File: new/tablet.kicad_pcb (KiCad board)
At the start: 2 copper layers, 15 parts, among them J1 Conn_02x20_Odd_Even, J2 USB_B_Micro, J3 Conn_02x04_Odd_Even, J4 Conn_02x04_Odd_Even, U1 STM32F429Z_E-G_Tx

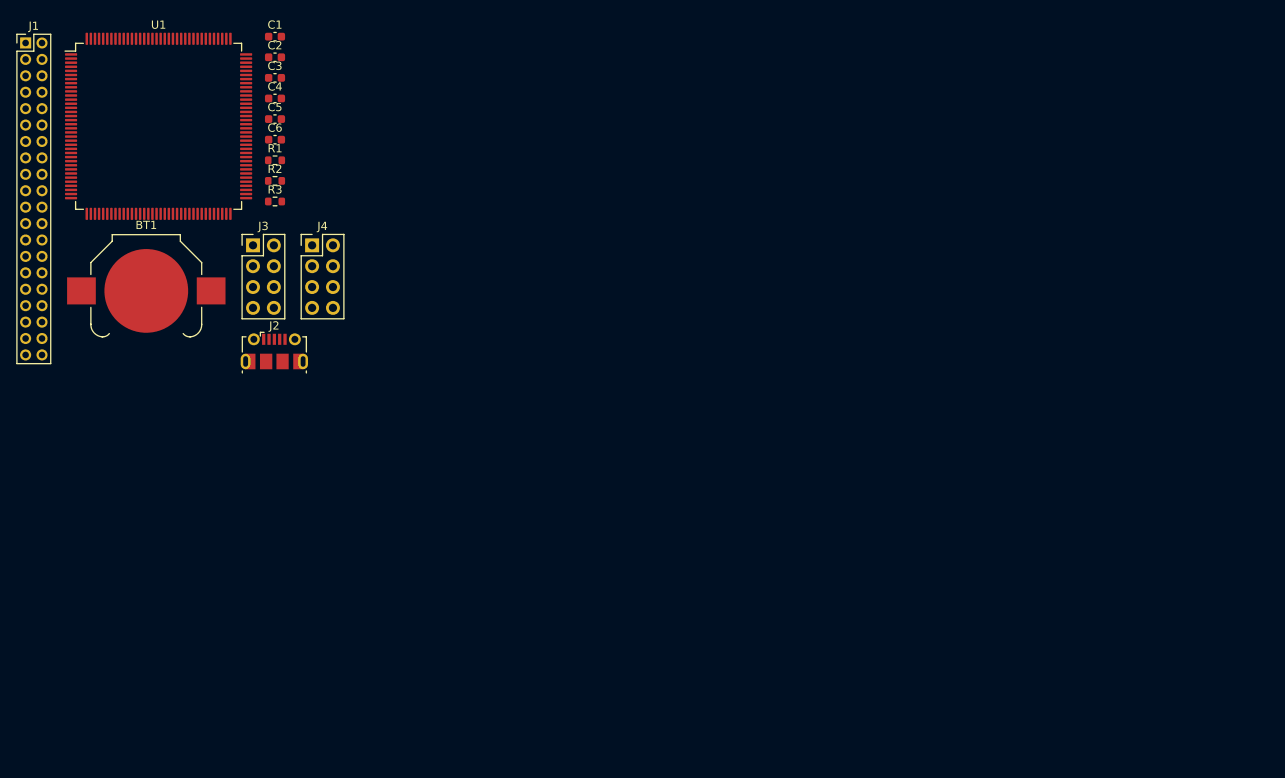
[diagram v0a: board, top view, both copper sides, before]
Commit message: place header on pcb
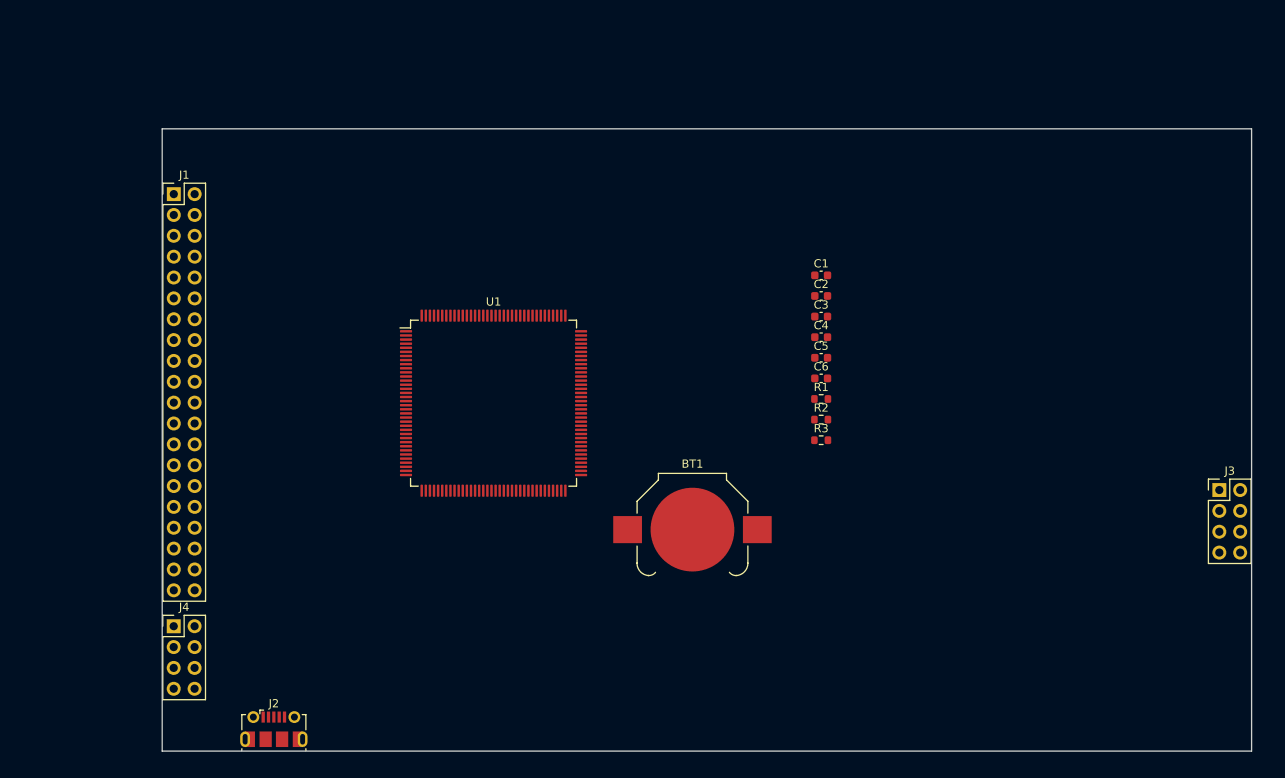
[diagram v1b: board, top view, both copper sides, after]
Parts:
- J1: footprint Connector_PinHeader_2.00mm:PinHeader_2x20_P2.00mm_Vertical -> Connector_PinHeader_2.54mm:PinHeader_2x20_P2.54mm_Vertical
- moved J3 121.4 mm to (261.5, 119.8)
- moved BT1 72.6 mm to (197.3, 124.6)
- moved C1 72.6 mm to (213.0, 93.7)
- moved C2 72.6 mm to (213.0, 96.2)
- moved C3 72.6 mm to (213.0, 98.7)
- moved C4 72.6 mm to (213.0, 101.2)
- moved C5 72.6 mm to (213.0, 103.7)
- moved C6 72.6 mm to (213.0, 106.2)
- moved R1 72.6 mm to (213.0, 108.7)
- moved R2 72.6 mm to (213.0, 111.2)
- moved R3 72.6 mm to (213.0, 113.7)
- moved U1 52.9 mm to (173.1, 109.2)
- moved J4 49.4 mm to (134.1, 136.4)
- moved J2 46.0 mm to (146.3, 148.9)
- moved J1 25.8 mm to (134.1, 83.8)
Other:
- board outline added: 132.7 x 75.8 mm

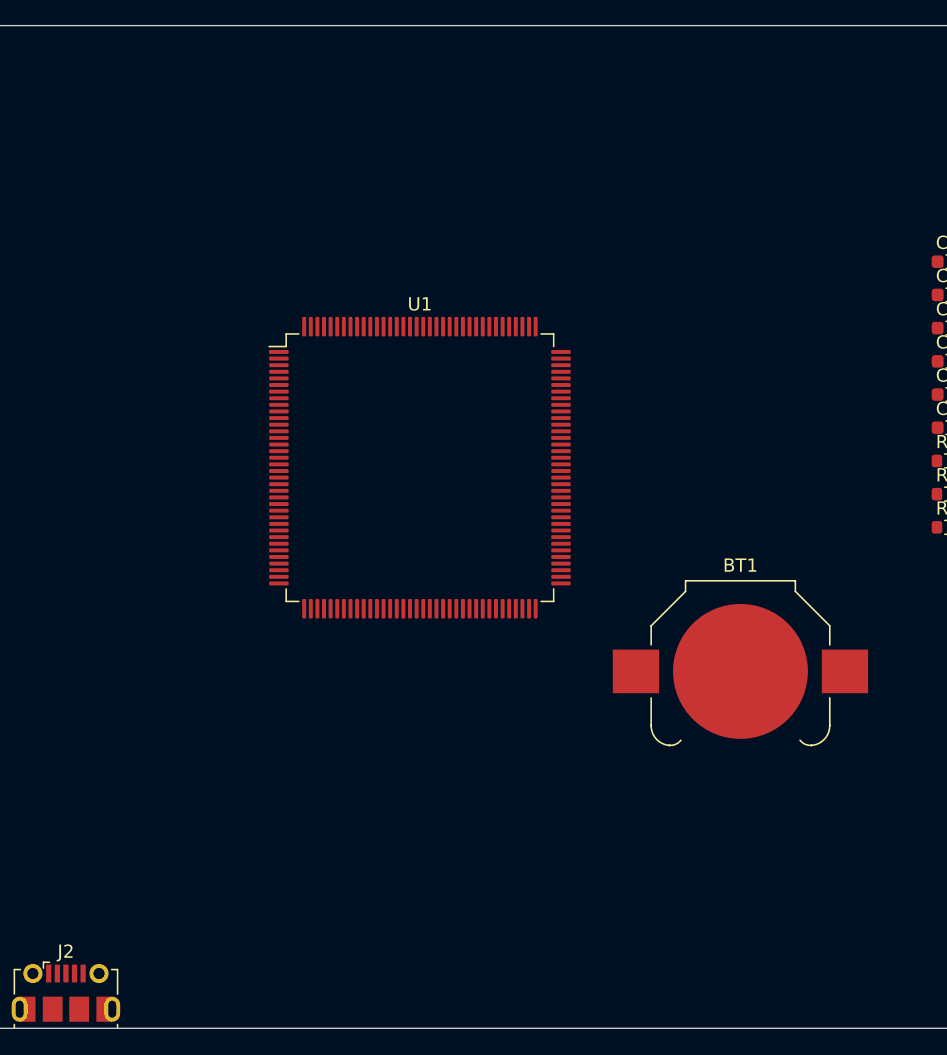
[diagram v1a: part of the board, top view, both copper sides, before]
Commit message: add TPS63001
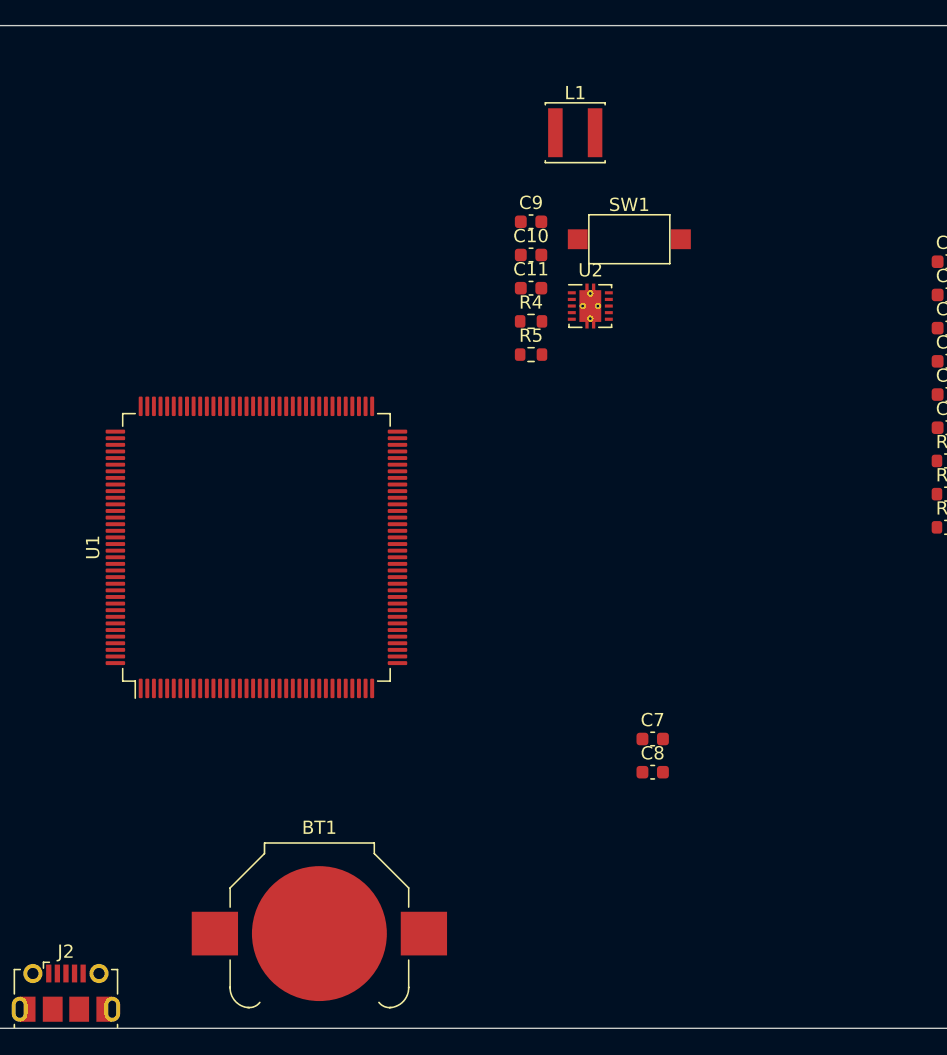
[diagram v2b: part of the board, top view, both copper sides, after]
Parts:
- added C10: 0.1uF, Capacitor_SMD:C_0603_1608Metric, F.Cu at (181.5, 93.1)
- added C11: 0.1uF, Capacitor_SMD:C_0603_1608Metric, F.Cu at (181.5, 95.7)
- added C7: 2.2uF, Capacitor_SMD:C_0603_1608Metric, F.Cu at (190.7, 129.7)
- added C8: 2.2uF, Capacitor_SMD:C_0603_1608Metric, F.Cu at (190.7, 132.2)
- added C9: 0.1uF, Capacitor_SMD:C_0603_1608Metric, F.Cu at (181.5, 90.6)
- added L1: LPS4012-103MRB, Inductor_SMD:L_Sunlord_SWPA4012S, F.Cu at (184.8, 83.9)
- added R4: 10k, Resistor_SMD:R_0603_1608Metric, F.Cu at (181.5, 98.2)
- added R5: 100, Resistor_SMD:R_0603_1608Metric, F.Cu at (181.5, 100.7)
- added SW1: SW_SPST, Button_Switch_SMD:SW_SPST_CK_RS282G05A3, F.Cu at (188.9, 92.0)
- added U2: TPS63001, Package_SON:Texas_DRC0010J_ThermalVias, F.Cu at (185.9, 97.0)
- J1: value Conn_02x20_Odd_Even -> FSMC/TOUCH-SPI
- J3: value Conn_02x04_Odd_Even -> SD/CARD
- J4: value Conn_02x04_Odd_Even -> FLASH/FONT
- moved BT1 37.5 mm to (165.5, 144.4)
- moved U1 13.7 mm to (160.7, 115.2), turned to 90 degrees
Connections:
- J1 pad 1: unconnected-(J1-Pin_1-Pad1) -> GND
- J1 pad 17: unconnected-(J1-Pin_17-Pad17) -> PD10-D15
- J1 pad 18: unconnected-(J1-Pin_18-Pad18) -> PD9-D14
- J1 pad 19: unconnected-(J1-Pin_19-Pad19) -> PD8-D13
- J1 pad 2: unconnected-(J1-Pin_2-Pad2) -> PA10-BL
- J1 pad 20: unconnected-(J1-Pin_20-Pad20) -> PE15-D12
- J1 pad 21: unconnected-(J1-Pin_21-Pad21) -> PE14-D11
- J1 pad 22: unconnected-(J1-Pin_22-Pad22) -> PE13-D10
- J1 pad 23: unconnected-(J1-Pin_23-Pad23) -> PE12-D9
- J1 pad 24: unconnected-(J1-Pin_24-Pad24) -> PE11-D8
- J1 pad 25: unconnected-(J1-Pin_25-Pad25) -> PE10-D7
- J1 pad 26: unconnected-(J1-Pin_26-Pad26) -> PE9-D6
- J1 pad 27: unconnected-(J1-Pin_27-Pad27) -> PE8-D5
- J1 pad 28: unconnected-(J1-Pin_28-Pad28) -> PE7-D4
- J1 pad 29: unconnected-(J1-Pin_29-Pad29) -> PD1-D3
- J1 pad 3: unconnected-(J1-Pin_3-Pad3) -> PD6-TP/IRQ
- J1 pad 30: unconnected-(J1-Pin_30-Pad30) -> PD0-D2
- J1 pad 31: unconnected-(J1-Pin_31-Pad31) -> PD15-D1
- J1 pad 32: unconnected-(J1-Pin_32-Pad32) -> PD14-D0
- J1 pad 33: unconnected-(J1-Pin_33-Pad33) -> TE
- J1 pad 34: unconnected-(J1-Pin_34-Pad34) -> TFT-RESET
- J1 pad 35: unconnected-(J1-Pin_35-Pad35) -> PD5-/WR
- J1 pad 36: unconnected-(J1-Pin_36-Pad36) -> PD4-/RD
- J1 pad 37: unconnected-(J1-Pin_37-Pad37) -> PD11-RS
- J1 pad 38: unconnected-(J1-Pin_38-Pad38) -> PD7-/CS
- J1 pad 39: unconnected-(J1-Pin_39-Pad39) -> +3V3
- J1 pad 40: unconnected-(J1-Pin_40-Pad40) -> GND
- J1 pad 5: unconnected-(J1-Pin_5-Pad5) -> PB14-SO
- J1 pad 6: unconnected-(J1-Pin_6-Pad6) -> PB15-SI
- J1 pad 7: unconnected-(J1-Pin_7-Pad7) -> PB13-TP/SCK
- J1 pad 8: unconnected-(J1-Pin_8-Pad8) -> PB12-TP/CS
- J3 pad 1: unconnected-(J3-Pin_1-Pad1) -> PC11-DAT3
- J3 pad 2: unconnected-(J3-Pin_2-Pad2) -> PC10-DAT2
- J3 pad 3: unconnected-(J3-Pin_3-Pad3) -> PC12-CLK
- J3 pad 4: unconnected-(J3-Pin_4-Pad4) -> PD2-CMD
- J3 pad 5: unconnected-(J3-Pin_5-Pad5) -> PC8-DAT0
- J3 pad 6: unconnected-(J3-Pin_6-Pad6) -> GND
- J3 pad 7: unconnected-(J3-Pin_7-Pad7) -> PC0-SDDETECT
- J3 pad 8: unconnected-(J3-Pin_8-Pad8) -> PC9-DAT1
- U1 pad 102: unconnected-(U1-PA10-Pad102) -> PA10-BL
- U1 pad 106: unconnected-(U1-VCAP_2-Pad106) -> Net-(U1-VCAP_2)
- U1 pad 111: unconnected-(U1-PC10-Pad111) -> PC10-DAT2
- U1 pad 112: unconnected-(U1-PC11-Pad112) -> PC11-DAT3
- U1 pad 113: unconnected-(U1-PC12-Pad113) -> PC12-CLK
- U1 pad 114: unconnected-(U1-PD0-Pad114) -> PD0-D2
- U1 pad 115: unconnected-(U1-PD1-Pad115) -> PD1-D3
- U1 pad 116: unconnected-(U1-PD2-Pad116) -> PD2-CMD
- U1 pad 118: unconnected-(U1-PD4-Pad118) -> PD4-/RD
- U1 pad 119: unconnected-(U1-PD5-Pad119) -> PD5-/WR
- U1 pad 122: unconnected-(U1-PD6-Pad122) -> PD6-TP/IRQ
- U1 pad 123: unconnected-(U1-PD7-Pad123) -> PD7-/CS
- U1 pad 138: unconnected-(U1-BOOT0-Pad138) -> BOOT0
- U1 pad 143: unconnected-(U1-PDR_ON-Pad143) -> +3V3
- U1 pad 25: unconnected-(U1-NRST-Pad25) -> Net-(U1-NRST)
- U1 pad 26: unconnected-(U1-PC0-Pad26) -> PC0-SDDETECT
- U1 pad 48: unconnected-(U1-PB2-Pad48) -> BOOT1
- U1 pad 58: unconnected-(U1-PE7-Pad58) -> PE7-D4
- U1 pad 59: unconnected-(U1-PE8-Pad59) -> PE8-D5
- U1 pad 60: unconnected-(U1-PE9-Pad60) -> PE9-D6
- U1 pad 63: unconnected-(U1-PE10-Pad63) -> PE10-D7
- U1 pad 64: unconnected-(U1-PE11-Pad64) -> PE11-D8
- U1 pad 65: unconnected-(U1-PE12-Pad65) -> PE12-D9
- U1 pad 66: unconnected-(U1-PE13-Pad66) -> PE13-D10
- U1 pad 67: unconnected-(U1-PE14-Pad67) -> PE14-D11
- U1 pad 68: unconnected-(U1-PE15-Pad68) -> PE15-D12
- U1 pad 71: unconnected-(U1-VCAP_1-Pad71) -> Net-(U1-VCAP_1)
- U1 pad 73: unconnected-(U1-PB12-Pad73) -> PB12-TP/CS
- U1 pad 74: unconnected-(U1-PB13-Pad74) -> PB13-TP/SCK
- U1 pad 75: unconnected-(U1-PB14-Pad75) -> PB14-SO
- U1 pad 76: unconnected-(U1-PB15-Pad76) -> PB15-SI
- U1 pad 77: unconnected-(U1-PD8-Pad77) -> PD8-D13
- U1 pad 78: unconnected-(U1-PD9-Pad78) -> PD9-D14
- U1 pad 79: unconnected-(U1-PD10-Pad79) -> PD10-D15
- U1 pad 80: unconnected-(U1-PD11-Pad80) -> PD11-RS
- U1 pad 85: unconnected-(U1-PD14-Pad85) -> PD14-D0
- U1 pad 98: unconnected-(U1-PC8-Pad98) -> PC8-DAT0
- U1 pad 99: unconnected-(U1-PC9-Pad99) -> PC9-DAT1

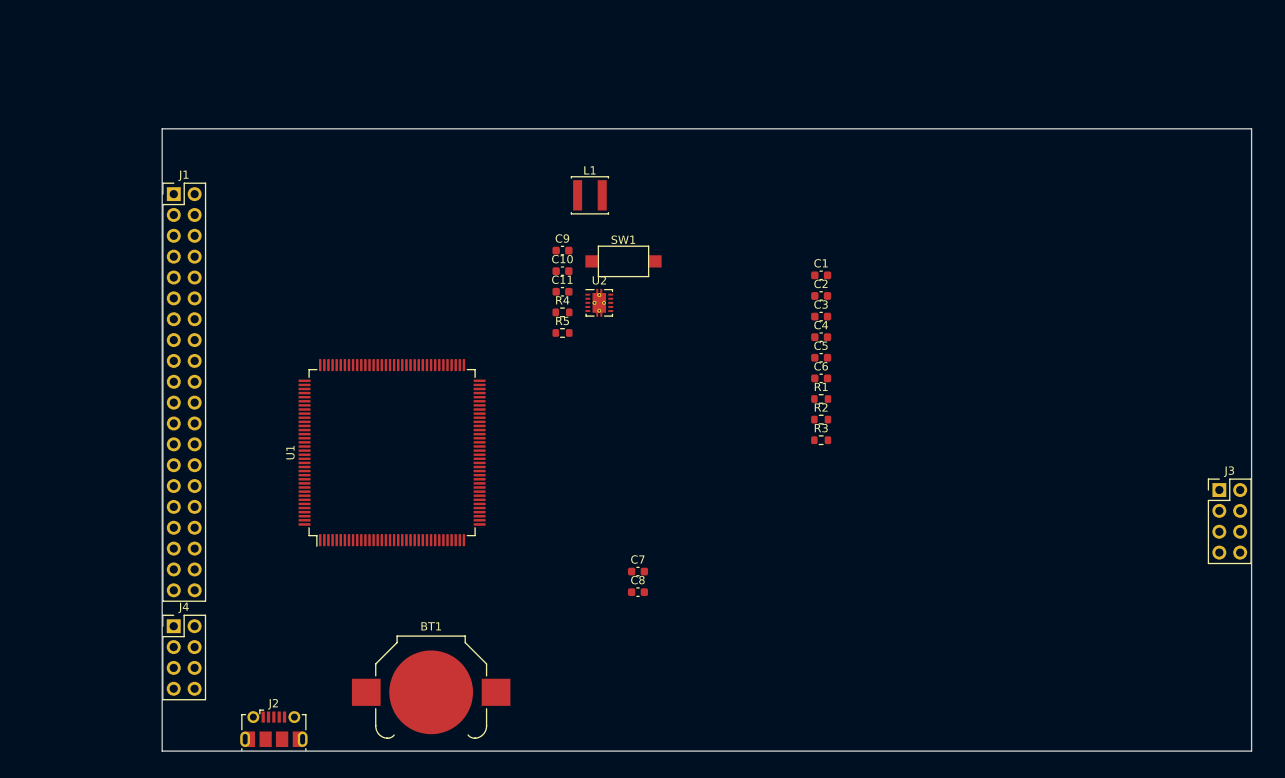
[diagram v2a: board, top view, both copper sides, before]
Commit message: add wiring + battery charging
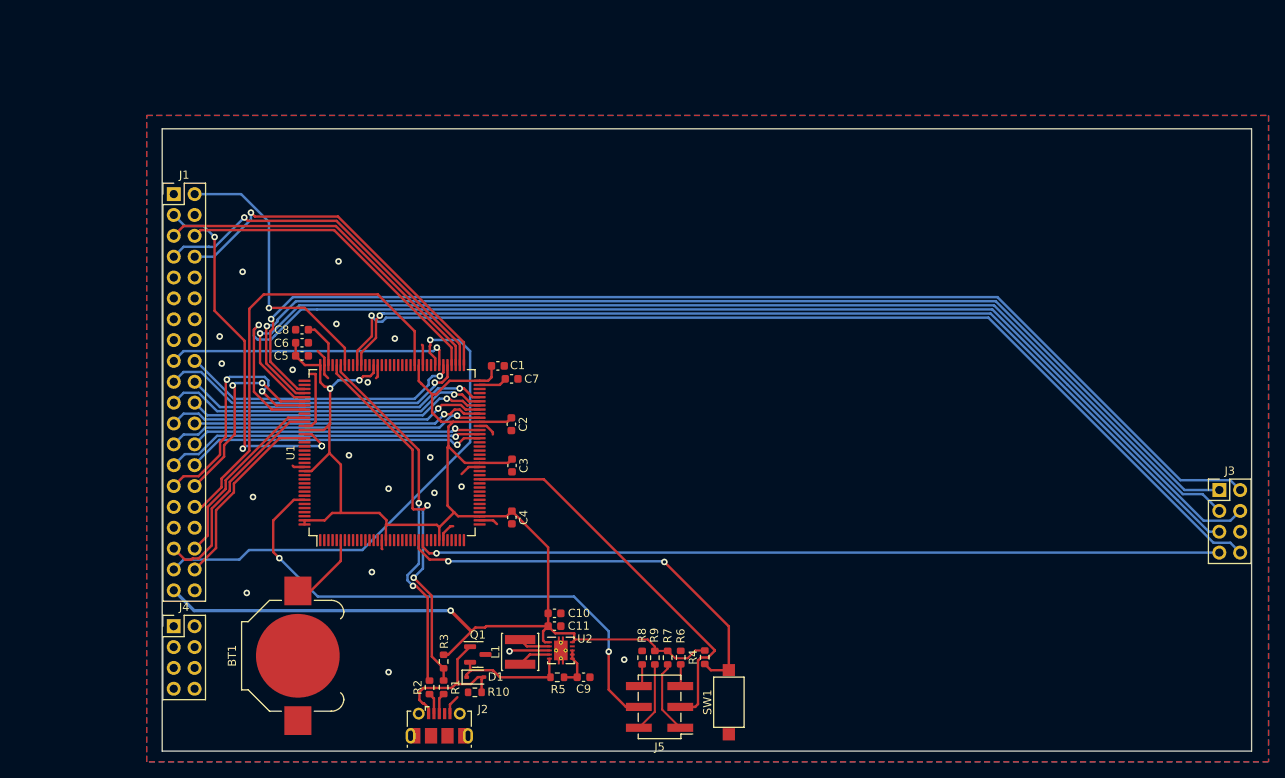
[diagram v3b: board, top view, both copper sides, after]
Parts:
- added D1: BAT48JFILM, Diode_SMD:D_SOD-323, F.Cu at (170.8, 142.6)
- added J5: Conn_02x03_Odd_Even, Connector_PinHeader_2.54mm:PinHeader_2x03_P2.54mm_Vertical_SMD, F.Cu at (193.3, 146.2)
- added Q1: DMG2301L, Package_TO_SOT_SMD:SOT-23, F.Cu at (171.1, 139.8)
- added R10: 10k, Resistor_SMD:R_0603_1608Metric, F.Cu at (170.8, 144.4)
- added R6: 10k, Resistor_SMD:R_0603_1608Metric, F.Cu at (195.9, 140.2)
- added R7: 10k, Resistor_SMD:R_0603_1608Metric, F.Cu at (194.3, 140.2)
- added R8: 10k, Resistor_SMD:R_0603_1608Metric, F.Cu at (191.2, 140.2)
- added R9: 10k, Resistor_SMD:R_0603_1608Metric, F.Cu at (192.7, 140.2)
- moved C6 63.4 mm to (149.7, 101.9)
- moved C5 63.2 mm to (149.7, 103.5)
- moved R1 57.9 mm to (167.0, 143.8), turned to 90 degrees
- moved R2 57.8 mm to (165.3, 143.8), turned to 90 degrees
- moved L1 56.3 mm to (176.3, 139.5), turned to 90 degrees
- moved SW1 55.2 mm to (201.7, 145.7), turned to 90 degrees
- moved R3 53.3 mm to (167.0, 140.7), turned to 90 degrees
- moved C9 52.0 mm to (184.0, 142.6)
- moved C8 51.9 mm to (149.7, 100.3), turned to 180 degrees
- moved R4 45.4 mm to (198.8, 140.2), turned to 90 degrees
- moved C4 43.6 mm to (175.3, 123.1), turned to -90 degrees
- moved U2 42.6 mm to (181.3, 139.3)
- moved R5 41.9 mm to (180.8, 142.6)
- moved C3 41.8 mm to (175.3, 116.8), turned to -90 degrees
- moved C10 41.7 mm to (180.5, 134.8)
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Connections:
- net BAT+ renamed Net-(D1-K)
- C10 pad 1: VCC -> +3V3
- C11 pad 1: VCC -> +3V3
- J2 pad 1: +5V -> VBUS
- R4 pad 1: +3V3 -> Net-(SW1-B)
- R4 pad 2: Net-(U1-NRST) -> +3V3
- SW1 pad 2: +3V3 -> Net-(SW1-B)
- U1 pad 103: unconnected-(U1-PA11-Pad103) -> PA11
- U1 pad 104: unconnected-(U1-PA12-Pad104) -> PA12
- U1 pad 25: Net-(U1-NRST) -> Net-(SW1-B)
- U2 pad 1: VCC -> +3V3
- U2 pad 10: VCC -> +3V3
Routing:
- net +3V3: track 0.00 -> 210.9 mm, vias 0 -> 3
- net PD2-CMD: track 0.00 -> 150.0 mm, vias 0 -> 1
- net PC10-DAT2: track 0.00 -> 139.9 mm, vias 0 -> 1
- net PC12-CLK: track 0.00 -> 139.4 mm, vias 0 -> 1
- net PC11-DAT3: track 0.00 -> 137.7 mm, vias 0 -> 1
- net PC9-DAT1: track 0.00 -> 125.0 mm, vias 0 -> 1
- net PC8-DAT0: track 0.00 -> 120.3 mm, vias 0 -> 1
- net PC0-SDDETECT: track 0.00 -> 98.2 mm, vias 0 -> 1
- net BOOT0: track 0.00 -> 65.2 mm, vias 0 -> 2
- net PD11-RS: track 0.00 -> 62.4 mm, vias 0 -> 1
- net PD14-D0: track 0.00 -> 54.3 mm
- net Net-(SW1-B): track 0.00 -> 51.3 mm, vias 0 -> 2
- net BOOT1: track 0.00 -> 47.5 mm
- net PA12: track 0.00 -> 46.9 mm, vias 0 -> 2
- net PD6-TP/IRQ: track 0.00 -> 46.1 mm, vias 0 -> 4
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- added copper zone on B.Cu, net GND
- added copper zone on F.Cu, net GND

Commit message: wiring
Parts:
- added C12: 0.1uF, Capacitor_SMD:C_0603_1608Metric, F.Cu at (183.6, 147.1)
- added C13: 0.1uF, Capacitor_SMD:C_0603_1608Metric, F.Cu at (172.7, 146.8)
- added C14: 0.1uF, Capacitor_SMD:C_0603_1608Metric, F.Cu at (170.9, 129.8)
- added C15: 0.1uF, Capacitor_SMD:C_0603_1608Metric, F.Cu at (155.4, 130.0)
- added D2: LED_Small, Resistor_SMD:R_0603_1608Metric, F.Cu at (179.3, 148.8)
- added J6: Conn_01x02, Connector_PinSocket_2.54mm:PinSocket_1x02_P2.54mm_Vertical, F.Cu at (182.9, 149.6)
- added J7: Conn_ARM_SWD_TagConnect_TC2030, Connector_PinHeader_2.54mm:PinHeader_1x06_P2.54mm_Vertical, F.Cu at (149.1, 78.5)
- added R11: 2k, Resistor_SMD:R_0603_1608Metric, F.Cu at (175.0, 149.4)
- added R12: 2k, Resistor_SMD:R_0603_1608Metric, F.Cu at (179.3, 147.1)
- added TP1: VIN, Connector_Wire:SolderWirePad_1x01_SMD_1x2mm, F.Cu at (176.5, 144.0)
- added U3: MCP73811T-420I-OT, Package_TO_SOT_SMD:SOT-23-5, F.Cu at (175.5, 146.8)
- added Y1: Crystal, Crystal:Crystal_SMD_HC49-SD, F.Cu at (163.1, 130.6)
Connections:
- net Net-(SW1-B) renamed RESET
- U1 pad 105: unconnected-(U1-PA13-Pad105) -> PA13-SWDIO
- U1 pad 109: unconnected-(U1-PA14-Pad109) -> PA14-SWCLK
- U1 pad 133: unconnected-(U1-PB3-Pad133) -> PB3-SWO
- U1 pad 23: unconnected-(U1-PH0-Pad23) -> PH0
- U1 pad 24: unconnected-(U1-PH1-Pad24) -> PH1
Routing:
- net RESET: track 51.3 -> 124.3 mm
- net PB3-SWO: track 0.00 -> 62.1 mm, vias 0 -> 4
- net +3V3: track 210.9 -> 255.2 mm, vias 3 -> 4
- net PA14-SWCLK: track 0.00 -> 39.4 mm, vias 0 -> 1
- net PA13-SWDIO: track 0.00 -> 26.9 mm, vias 0 -> 4
- net Net-(BT1-+): track 9.28 -> 33.4 mm
- net +BATT: track 0.00 -> 21.8 mm, vias 0 -> 2
- net PH0: track 0.00 -> 11.3 mm
- net PH1: track 0.00 -> 11.2 mm
- net VBUS: track 18.9 -> 28.8 mm
- net GND: track 35.5 -> 41.0 mm, vias 13 -> 29
- net Net-(U3-CE): track 0.00 -> 2.14 mm
- net Net-(D1-K): track 14.4 -> 16.5 mm
- net Net-(D2-K): track 0.00 -> 1.78 mm
- net Net-(U3-PROG): track 0.00 -> 1.67 mm
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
